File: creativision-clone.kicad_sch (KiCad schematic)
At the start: 81 parts, among them J1 Conn_01x10_Socket, J2 Conn_01x10_Socket, J3 Conn_01x07_Pin, J4 Conn_01x04_Socket, P1 Cartridge Slot, SW1 Reset, U1 AS6C62256-DIP, U100 74HCT574, U101 74HCT574, U102 74HCT574, U12 74LS32, U15 74LS139, U18 AS6C62256-DIP, U2 6502, U20 27256, U21 6821, U22 SN76489AN, U3 TMS9918A, U99 74HCT04, X1 2MHz

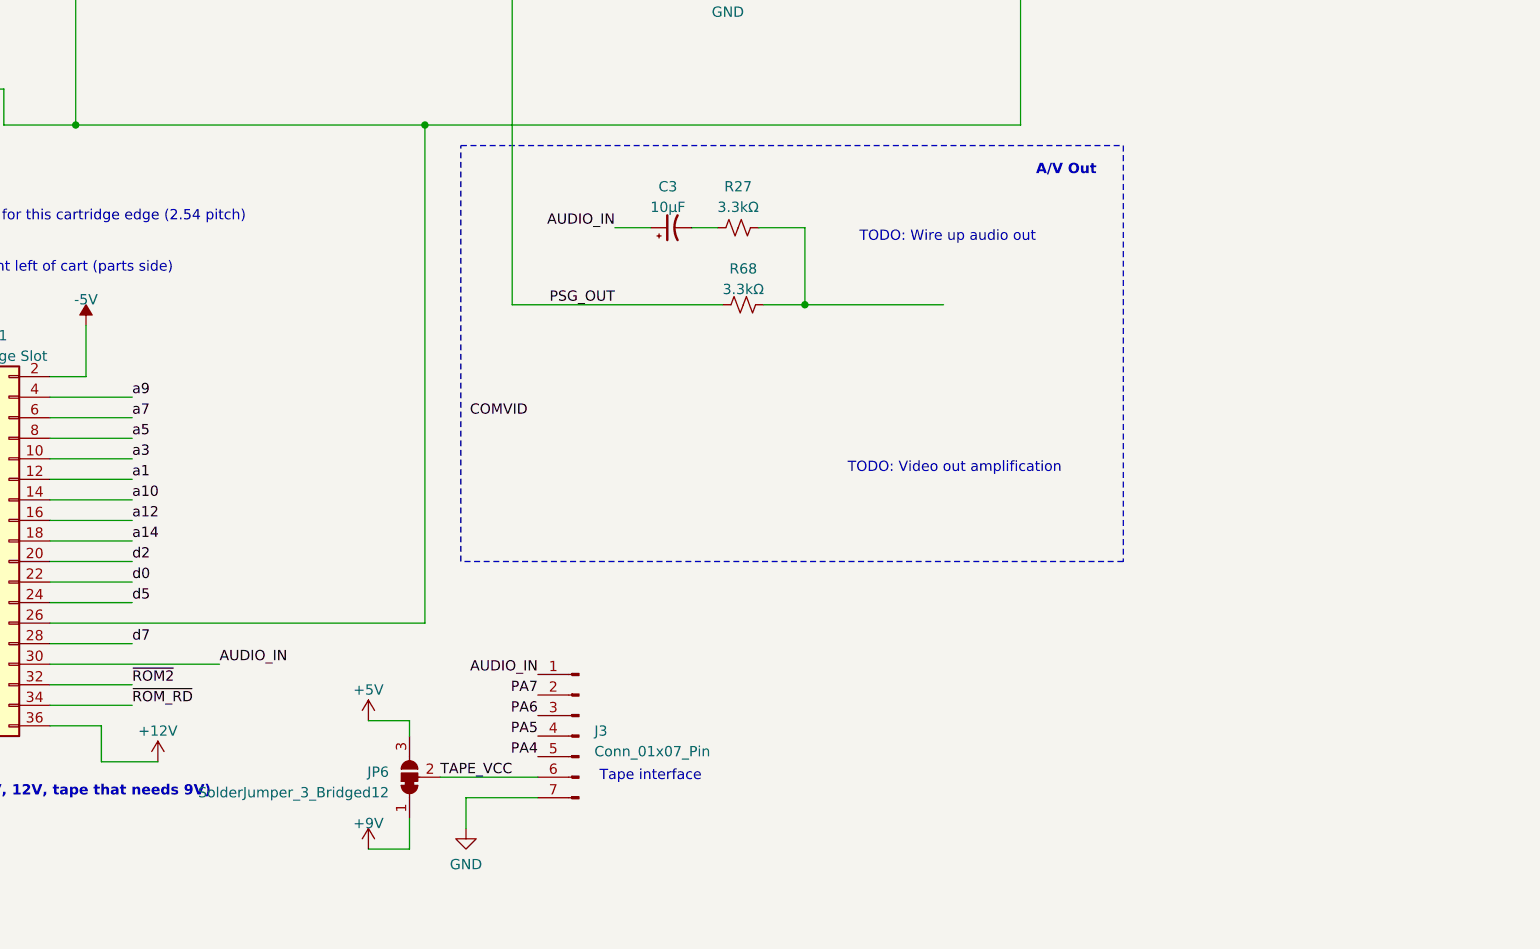
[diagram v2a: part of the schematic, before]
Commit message: Audio out
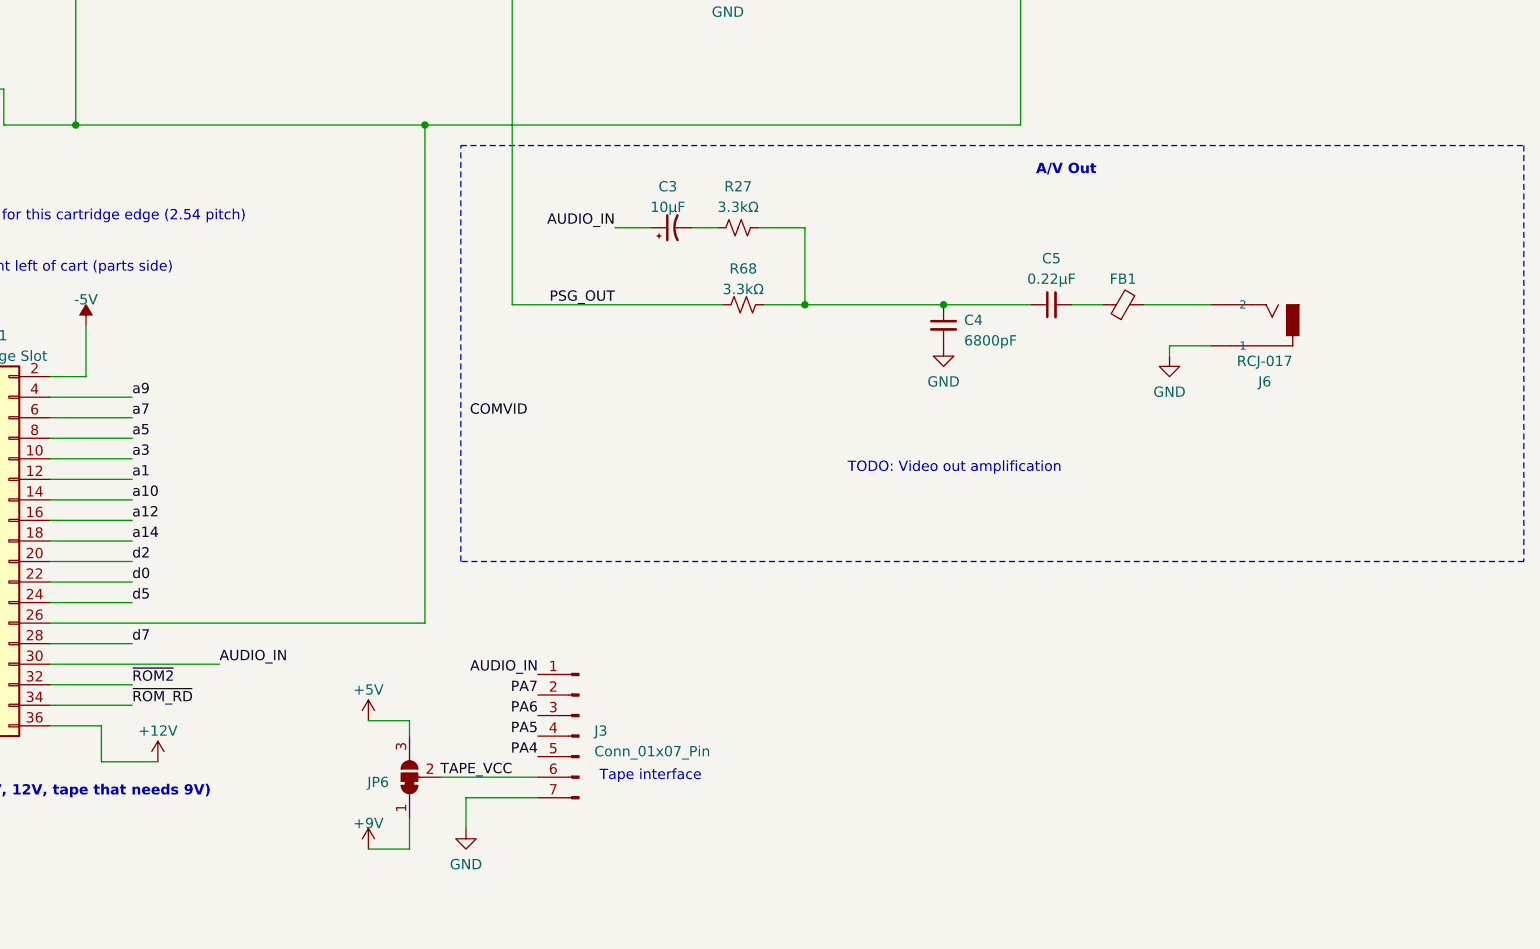
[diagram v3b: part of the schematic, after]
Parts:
- added C4: 6800pF, symbol Device:C_Small
- added C5: 0.22µF, symbol Device:C_Small
- added FB1: FerriteBead_Small, symbol Device:FerriteBead_Small
- added J6: RCJ-017, CUI_RCJ-017, symbol RCJ-017:RCJ-017
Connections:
- net GND: now also C4.2, J6.1A (1), J6.1B (1), J6.1C (1)
- net at R27.2, R68.2: now also C4.1, C5.1
- new net: C5.2, FB1.1
- new net: FB1.2, J6.2
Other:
- note removed: "TODO: Wire up audio out"
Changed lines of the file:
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@@
   (junction (at 330.2 38.1) (diameter 0) (color 0 0 0 0)
   )
+  (junction (at 342.9 165.735) (diameter 0) (color 0 0 0 0)
+  )
   (junction (at 353.695 41.91) (diameter 0) (color 0 0 0 0)
   )
@@
     (stroke (width 0) (type default))
   )
+  (wire (pts (xy 358.775 165.735) (xy 362.585 165.735))
+    (stroke (width 0) (type default))
+  )
   (wire (pts (xy 310.515 84.455) (xy 310.515 73.025))
     (stroke (width 0) (type default))
@@
     (stroke (width 0) (type default))
   )
+  (wire (pts (xy 370.84 172.085) (xy 370.84 170.815))
+    (stroke (width 0) (type default))
+  )
   (wire (pts (xy 323.85 38.1) (xy 300.355 38.1))
     (stroke (width 0) (type default))
@@
     (stroke (width 0) (type default))
   )
+  (wire (pts (xy 367.665 165.735) (xy 375.92 165.735))
+    (stroke (width 0) (type default))
+  )
   (wire (pts (xy 319.405 113.665) (xy 289.56 113.665))
     (stroke (width 0) (type default))
@@
     (stroke (width 0) (type default))
   )
+  (wire (pts (xy 370.84 170.815) (xy 375.92 170.815))
+    (stroke (width 0) (type default))
+  )
   (wire (pts (xy 142.875 66.04) (xy 142.875 71.755))
     (stroke (width 0) (type default))
@@
     (stroke (width 0) (type default))
   )
+  (wire (pts (xy 342.9 165.735) (xy 353.695 165.735))
+    (stroke (width 0) (type default))
+  )
   (wire (pts (xy 287.655 54.61) (xy 287.655 57.15))
     (stroke (width 0) (type default))
@@
     (stroke (width 0) (type default))
   )
-  (rectangle (start 283.21 146.05) (end 365.125 197.485)
+  (rectangle (start 283.21 146.05) (end 414.655 197.485)
     (stroke (width 0) (type dot))
     (fill (type none))
   )
-  (text "TODO: Wire up audio out" (at 354.33 158.115 0)
-    (effects (font (size 1.27 1.27)) (justify right bottom))
-  )
   (text "TODO: footprint for this cartridge edge (2.54 pitch)"
     (at 212.09 155.575 0)
@@
     )
   )
+  (symbol (lib_id "power:GND") (at 370.84 172.085 0) (unit 1)
+    (in_bom yes) (on_board yes) (dnp no) (fields_autoplaced)
+    (property "Reference" "#PWR061" (at 370.84 178.435 0)
+      (effects (font (size 1.27 1.27)) hide)
+    )
+    (property "Value" "GND" (at 370.84 176.53 0)
+      (effects (font (size 1.27 1.27)))
+    )
+    (property "Footprint" "" (at 370.84 172.085 0)
+      (effects (font (size 1.27 1.27)) hide)
+    )
+    (property "Datasheet" "" (at 370.84 172.085 0)
+      (effects (font (size 1.27 1.27)) hide)
+    )
+    (pin "1")
+    (instances
+      (project "creativision-clone"
+        (path "/4f154aad-bddd-4366-bec7-a527fffe24b1"
+          (reference "#PWR061") (unit 1)
+        )
+      )
+    )
+  )
   (symbol (lib_id "65xx:6502") (at 97.79 99.06 0) (unit 1)
     (in_bom yes) (on_board yes) (dnp no) (fields_autoplaced)
@@
   (symbol (lib_id "Jumper:SolderJumper_3_Bridged12") (at 276.86 224.155 90) (unit 1)
     (in_bom yes) (on_board yes) (dnp no) (fields_autoplaced)
-    (property "Reference" "JP6" (at 274.32 223.52 90)
+    (property "Reference" "JP6" (at 274.32 224.79 90)
       (effects (font (size 1.27 1.27)) (justify left))
     )
     (property "Value" "SolderJumper_3_Bridged12" (at 274.32 226.06 90)
-      (effects (font (size 1.27 1.27)) (justify left))
+      (effects (font (size 1.27 1.27)) (justify left) hide)
     )
     (property "Footprint" "" (at 276.86 224.155 0)
@@
     )
   )
+  (symbol (lib_id "power:GND") (at 342.9 170.815 0) (unit 1)
+    (in_bom yes) (on_board yes) (dnp no) (fields_autoplaced)
+    (property "Reference" "#PWR060" (at 342.9 177.165 0)
+      (effects (font (size 1.27 1.27)) hide)
+    )
+    (property "Value" "GND" (at 342.9 175.26 0)
+      (effects (font (size 1.27 1.27)))
+    )
+    (property "Footprint" "" (at 342.9 170.815 0)
+      (effects (font (size 1.27 1.27)) hide)
+    )
+    (property "Datasheet" "" (at 342.9 170.815 0)
+      (effects (font (size 1.27 1.27)) hide)
+    )
+    (pin "1")
+    (instances
+      (project "creativision-clone"
+        (path "/4f154aad-bddd-4366-bec7-a527fffe24b1"
+          (reference "#PWR060") (unit 1)
+        )
+      )
+    )
+  )
   (symbol (lib_id "power:+5V") (at 121.92 258.445 0) (unit 1)
     (in_bom yes) (on_board yes) (dnp no) (fields_autoplaced)
@@
     )
   )
+  (symbol (lib_id "Device:C_Small") (at 356.235 165.735 90) (unit 1)
+    (in_bom yes) (on_board yes) (dnp no) (fields_autoplaced)
+    (property "Reference" "C5" (at 356.2413 160.02 90)
+      (effects (font (size 1.27 1.27)))
+    )
+    (property "Value" "0.22µF" (at 356.2413 162.56 90)
+      (effects (font (size 1.27 1.27)))
+    )
+    (property "Footprint" "" (at 356.235 165.735 0)
+      (effects (font (size 1.27 1.27)) hide)
+    )
+    (property "Datasheet" "~" (at 356.235 165.735 0)
+      (effects (font (size 1.27 1.27)) hide)
+    )
+    (pin "1")
+    (pin "2")
+    (instances
+      (project "creativision-clone"
+        (path "/4f154aad-bddd-4366-bec7-a527fffe24b1"
+          (reference "C5") (unit 1)
+        )
+      )
+    )
+  )
   (symbol (lib_id "AS6C62256:AS6C62256-DIP") (at 248.285 261.62 0) (unit 1)
     (in_bom yes) (on_board yes) (dnp no) (fields_autoplaced)
@@
     )
   )
+  (symbol (lib_id "RCJ-017:RCJ-017") (at 383.54 168.275 180) (unit 1)
+    (in_bom yes) (on_board yes) (dnp no)
+    (property "Reference" "J6" (at 382.6129 175.26 0)
+      (effects (font (size 1.27 1.27)))
+    )
+    (property "Value" "RCJ-017" (at 382.6129 172.72 0)
+      (effects (font (size 1.27 1.27)))
+    )
+    (property "Footprint" "CUI_RCJ-017" (at 383.54 168.275 0)
+      (effects (font (size 1.27 1.27)) (justify left bottom) hide)
+    )
+    (property "Datasheet" "CUI Inc" (at 383.54 168.275 0)
+      (effects (font (size 1.27 1.27)) (justify left bottom) hide)
+    )
+    (property "" "Manufacturer recommendations" (at 383.54 168.275 0)
+      (effects (font (size 1.27 1.27)) (justify left bottom) hide)
+    )
+    (pin "1A")
+    (pin "1B")
+    (pin "1C")
+    (pin "2")
+    (instances
+      (project "creativision-clone"
+        (path "/4f154aad-bddd-4366-bec7-a527fffe24b1"
+          (reference "J6") (unit 1)
+        )
+      )
+    )
+  )
   (symbol (lib_id "power:-5V") (at 168.91 226.695 0) (unit 1)
     (in_bom yes) (on_board yes) (dnp no) (fields_autoplaced)
@@
         )
       )
+    )
+  )
+  (symbol (lib_id "Device:FerriteBead_Small") (at 365.125 165.735 90) (unit 1)
+    (in_bom yes) (on_board yes) (dnp no) (fields_autoplaced)
+    (property "Reference" "FB1" (at 365.0869 162.56 90)
+      (effects (font (size 1.27 1.27)))
+    )
+    (property "Value" "FerriteBead_Small" (at 365.0869 162.56 90)
+      (effects (font (size 1.27 1.27)) hide)
+    )
+    (property "Footprint" "" (at 365.125 167.513 90)
+      (effects (font (size 1.27 1.27)) hide)
+    )
+    (property "Datasheet" "~" (at 365.125 165.735 0)
+      (effects (font (size 1.27 1.27)) hide)
+    )
+    (pin "1")
+    (pin "2")
+    (instances
+      (project "creativision-clone"
+        (path "/4f154aad-bddd-4366-bec7-a527fffe24b1"
+          (reference "FB1") (unit 1)
+        )
+      )
+    )
+  )
+  (symbol (lib_id "Device:C_Small") (at 342.9 168.275 0) (unit 1)
+    (in_bom yes) (on_board yes) (dnp no) (fields_autoplaced)
+    (property "Reference" "C4" (at 345.44 167.6463 0)
+      (effects (font (size 1.27 1.27)) (justify left))
+    )
+    (property "Value" "6800pF" (at 345.44 170.1863 0)
+      (effects (font (size 1.27 1.27)) (justify left))
+    )
+    (property "Footprint" "" (at 342.9 168.275 0)
+      (effects (font (size 1.27 1.27)) hide)
+    )
+    (property "Datasheet" "~" (at 342.9 168.275 0)
+      (effects (font (size 1.27 1.27)) hide)
+    )
+    (pin "1")
+    (pin "2")
+    (instances
+      (project "creativision-clone"
+        (path "/4f154aad-bddd-4366-bec7-a527fffe24b1"
+          (reference "C4") (unit 1)
+        )
+      )

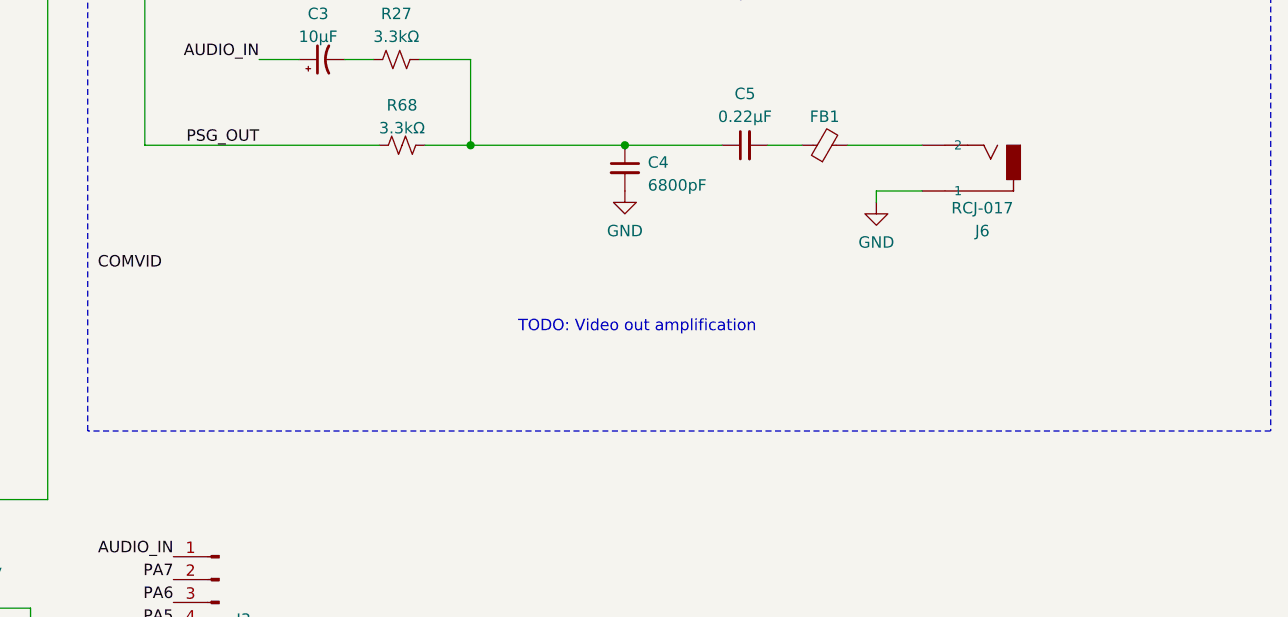
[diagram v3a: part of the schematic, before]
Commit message: AV out
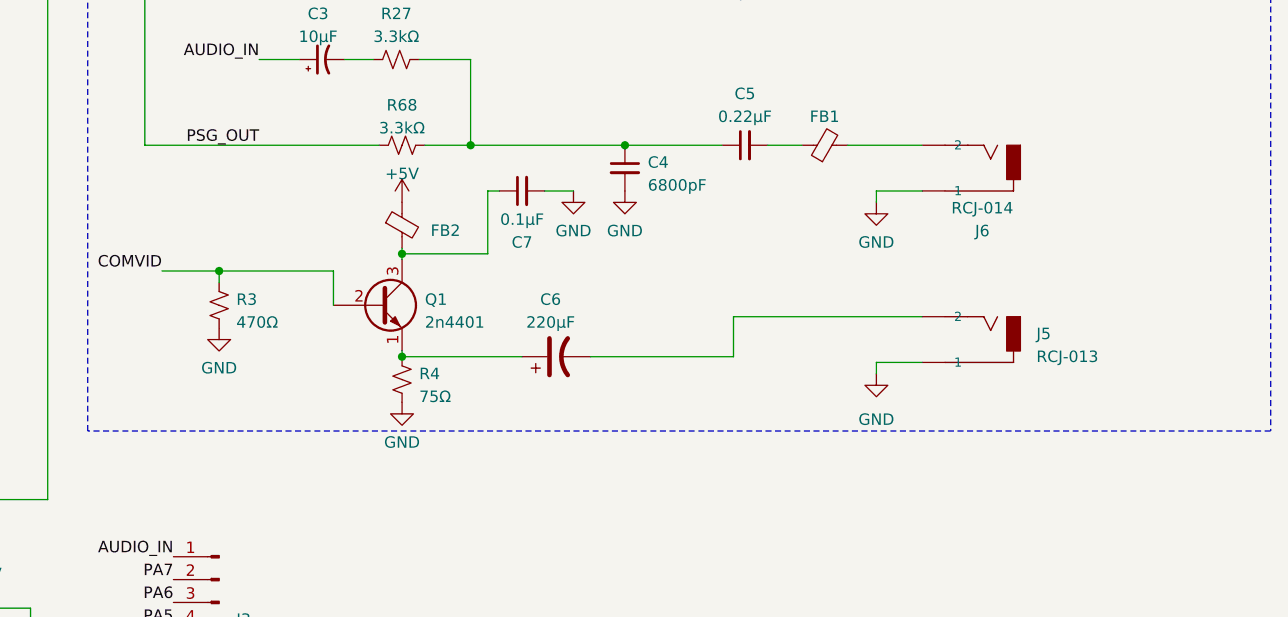
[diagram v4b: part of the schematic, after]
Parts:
- added C6: 220µF, symbol Device:C_Polarized_US
- added C7: 0.1µF, symbol Device:C_Small
- added FB2: FerriteBead_Small, symbol Device:FerriteBead_Small
- added J5: RCJ-013, CUI_RCJ-017, symbol RCJ-017:RCJ-017
- added Q1: 2n4401, symbol Device:Q_NPN_EBC
- added R3: 470Ω, symbol Device:R_Small_US
- added R4: 75Ω, symbol Device:R_Small_US
- J6: value RCJ-017 -> RCJ-014
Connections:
- net +5V: now also FB2.1
- net COMVID: now also Q1.2 (B), R3.1
- net GND: now also C7.2, J5.1A (1), J5.1B (1), J5.1C (1), R3.2, R4.2
- new net: C7.1, FB2.2, Q1.3 (C)
- new net: C6.1, Q1.1 (E), R4.1
- new net: C6.2, J5.2
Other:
- note removed: "TODO: Video out amplification"
